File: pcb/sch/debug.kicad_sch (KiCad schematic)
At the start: 1 part, among them J1 HIROSE_FH12-16S-0.5SH_55

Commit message: fices for boot definition
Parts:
- added J2: TC2030, Connector:Tag-Connect_TC2030-IDC-NL_2x03_P1.27mm_Vertical, symbol Connector:TC2030
- added R1301: 22, Resistor_SMD:R_0402_1005Metric, symbol Device:R_US
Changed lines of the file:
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@@
+		)
+	)
+	(text_box "implement boot strap to gnd for jtag mode here, on opposide end of this connector which will just have the digilent hs2/3 connector and a header for uart to access linux terminal"
+		(exclude_from_sim no)
+		(at 180.34 104.14 0)
+		(size 22.86 25.4)
+		(margins 0.9525 0.9525 0.9525 0.9525)
+		(stroke
+			(width 0)
+			(type solid)
+			(color 0 0 0 1)
+		)
+		(fill
+			(type none)
+		)
+		(effects
+			(font
+				(size 1.27 1.27)
+			)
+			(justify left top)
 		)
 	)
@@
 					(unit 1)
 				)
+			)
+		)
+	)
+	(symbol
+		(lib_id "Device:R_US")
+		(at 100.33 104.14 90)
+		(unit 1)
+		(body_style 1)
+		(exclude_from_sim no)
+		(in_bom yes)
+		(on_board yes)
+		(in_pos_files yes)
+		(dnp no)
+		(fields_autoplaced yes)
+		(property "Reference" "R1301"
+			(at 100.33 97.79 90)
+			(show_name no)
+			(do_not_autoplace no)
+			(effects
+				(font
+					(size 1.27 1.27)
+				)
+			)
+		)
+		(property "Value" "22"
+			(at 100.33 100.33 90)
+			(show_name no)
+			(do_not_autoplace no)
+			(effects
+				(font
+					(size 1.27 1.27)
+				)
+			)
+		)
+		(property "Footprint" "Resistor_SMD:R_0402_1005Metric"
+			(at 100.584 103.124 90)
+			(hide yes)
+			(show_name no)
+			(do_not_autoplace no)
+			(effects
+				(font
+					(size 1.27 1.27)
+				)
+			)
+		)
+		(property "Datasheet" ""
+			(at 100.33 104.14 0)
+			(hide yes)
+			(show_name no)
+			(do_not_autoplace no)
+			(effects
+				(font
+					(size 1.27 1.27)
+				)
+			)
+		)
+		(property "Description" ""
+			(at 100.33 104.14 0)
+			(hide yes)
+			(show_name no)
+			(do_not_autoplace no)
+			(effects
+				(font
+					(size 1.27 1.27)
+				)
+			)
+		)
+		(property "Manufacturer" ""
+			(at 100.33 104.14 0)
+			(hide yes)
+			(show_name no)
+			(do_not_autoplace no)
+			(effects
+				(font
+					(size 1.27 1.27)
+				)
+			)
+		)
+		(property "Manufacturer Product Number" ""
+			(at 100.33 104.14 0)
+			(hide yes)
+			(show_name no)
+			(do_not_autoplace no)
+			(effects
+				(font
+					(size 1.27 1.27)
+				)
+			)
+		)
+		(pin "1"
+		)
+		(pin "2"
+		)
+		(instances
+			(project "CUTIE-CITRUS"
+				(path "/875da261-7543-41df-9bd5-25bca104c872/1edff41f-1781-4ab1-8293-452f989504f2"
+					(reference "R1301")
+					(unit 1)
+				)
+			)
+		)
+	)
+	(symbol
+		(lib_id "Connector:TC2030")
+		(at 91.44 134.62 0)
+		(unit 1)
+		(body_style 1)
+		(exclude_from_sim no)
+		(in_bom no)
+		(on_board yes)
+		(in_pos_files yes)
+		(dnp no)
+		(fields_autoplaced yes)
+		(property "Reference" "J2"
+			(at 92.71 121.92 0)
+			(show_name no)
+			(do_not_autoplace no)
+			(effects
+				(font
+					(size 1.27 1.27)
+				)
+			)
+		)
+		(property "Value" "TC2030"
+			(at 92.71 124.46 0)
+			(show_name no)
+			(do_not_autoplace no)
+			(effects
+				(font
+					(size 1.27 1.27)
+				)
+			)
+		)
+		(property "Footprint" "Connector:Tag-Connect_TC2030-IDC-NL_2x03_P1.27mm_Vertical"
+			(at 92.71 134.62 0)
+			(hide yes)
+			(show_name no)
+			(do_not_autoplace no)
+			(effects
+				(font
+					(size 1.27 1.27)
+				)
+			)
+		)
+		(property "Datasheet" "https://www.tag-connect.com/wp-content/uploads/bsk-pdf-manager/2019/12/TC2030-IDC-NL-Datasheet-Rev-B.pdf"
+			(at 92.71 134.62 0)
+			(hide yes)
+			(show_name no)
+			(do_not_autoplace no)
+			(effects
+				(font
+					(size 1.27 1.27)
+				)
+			)
+		)
+		(property "Description" "Tag-Connect’s 6-pins connector"
+			(at 91.44 134.62 0)
+			(hide yes)
+			(show_name no)
+			(do_not_autoplace no)
+			(effects
+				(font
+					(size 1.27 1.27)
+				)
+			)
+		)
+		(pin "1"
+		)
+		(pin "3"
+		)
+		(pin "6"
+		)
+		(pin "5"
+		)
+		(pin "2"
+		)
+		(pin "4"
+		)
+		(instances
+			(project ""
+				(path "/875da261-7543-41df-9bd5-25bca104c872/1edff41f-1781-4ab1-8293-452f989504f2"
+					(reference "J2")
+					(unit 1)
+				)

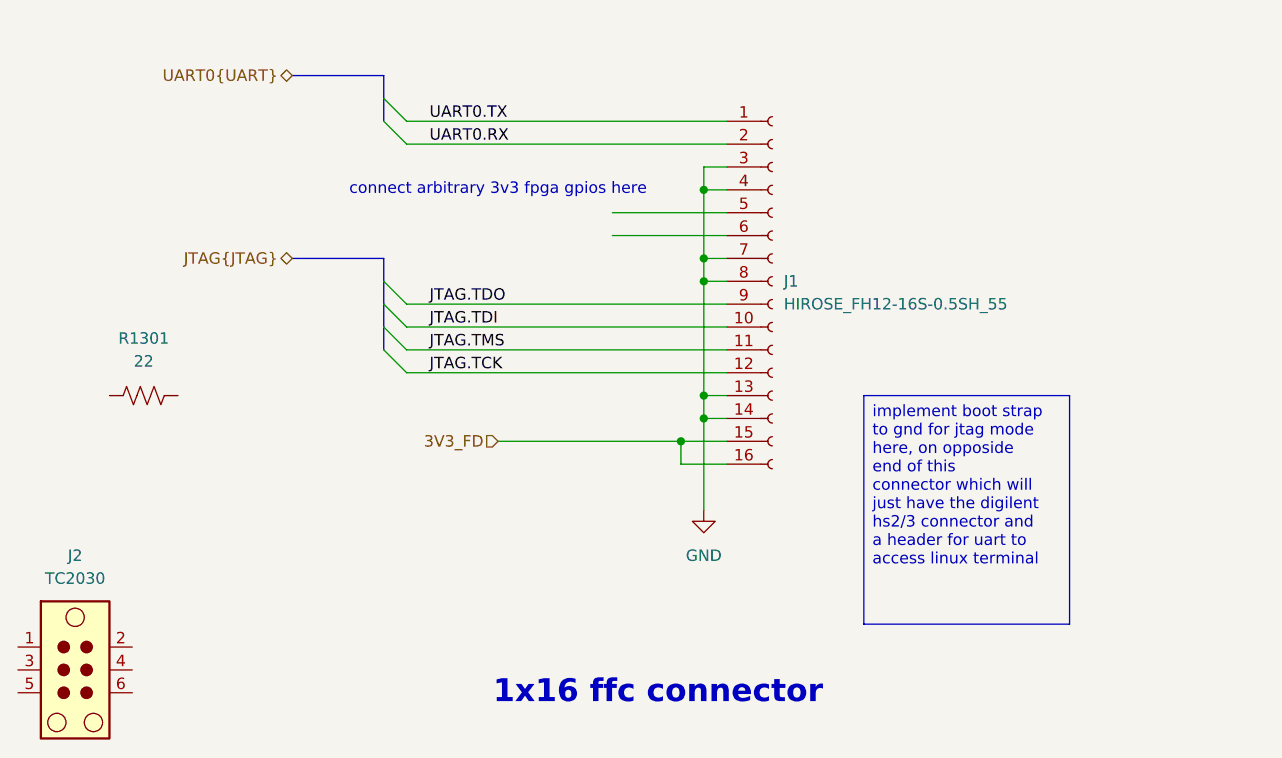
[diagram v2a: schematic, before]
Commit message: byte swapping and rough layout
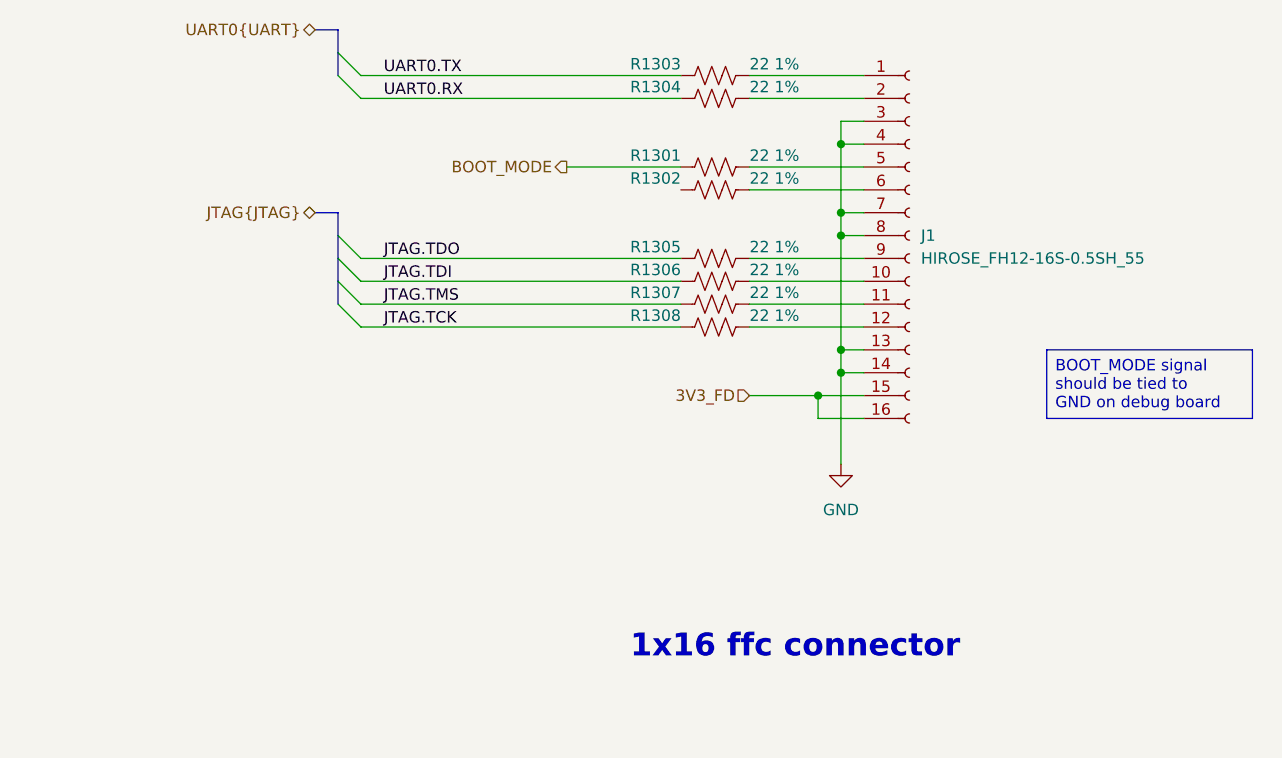
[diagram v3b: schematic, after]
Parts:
- removed J2: TC2030, Connector:Tag-Connect_TC2030-IDC-NL_2x03_P1.27mm_Vertical, symbol Connector:TC2030
- added R1302, R1303, R1304, R1305, R1306, R1307, R1308: 22 1%, Resistor_SMD:R_0402_1005Metric, symbol Device:R_US
- R1301: value 22 -> 22 1%
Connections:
- net JTAG.TCK: now also R1308.1; no longer J1.12 (Pin_12)
- net JTAG.TDI: now also R1306.1; no longer J1.10 (Pin_10)
- net JTAG.TDO: now also R1305.1; no longer J1.9 (Pin_9)
- net JTAG.TMS: now also R1307.1; no longer J1.11 (Pin_11)
- net UART0.RX: now also R1304.1; no longer J1.2 (Pin_2)
- net UART0.TX: now also R1303.1; no longer J1.1 (Pin_1)
- net at J1.5 (Pin_5): now also R1301.2
- net at J1.6 (Pin_6): now also R1302.2
- net BOOT_MODE: now reaches R1301.1
- new net: J1.12 (Pin_12), R1308.2
- new net: J1.1 (Pin_1), R1303.2
- new net: J1.10 (Pin_10), R1306.2
- new net: J1.11 (Pin_11), R1307.2
- new net: J1.2 (Pin_2), R1304.2
- new net: J1.9 (Pin_9), R1305.2
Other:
- note removed: "connect arbitrary 3v3 fpga gpios here"
- moved on the sheet: J1

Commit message: power
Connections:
- net 3V3_FD renamed 3V3_Z
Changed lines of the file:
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@@
 		)
 	)
-	(hierarchical_label "3V3_FD"
+	(hierarchical_label "3V3_Z"
 		(shape input)
 		(at 167.64 104.14 180)
